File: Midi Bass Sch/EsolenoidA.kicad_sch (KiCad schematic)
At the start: 105 parts, among them Q10 BDW93C, Q11 BDW93C, Q12 BDW93C, Q13 BDW93C, Q14 BDW93C, Q15 BDW93C, Q16 BDW93C, Q17 BDW93C, Q18 BDW93C, Q19 BDW93C, Q20 BDW93C, Q21 BDW93C, Q22 BDW93C, Q23 BDW93C, Q24 BDW93C, Q25 BDW93C, Q26 BDW93C, Q27 BDW93C, Q28 BDW93C, Q9 BDW93C, U10 LTV-247, U11 LTV-247, U4 LTV-247, U8 LTV-247, U9 LTV-247

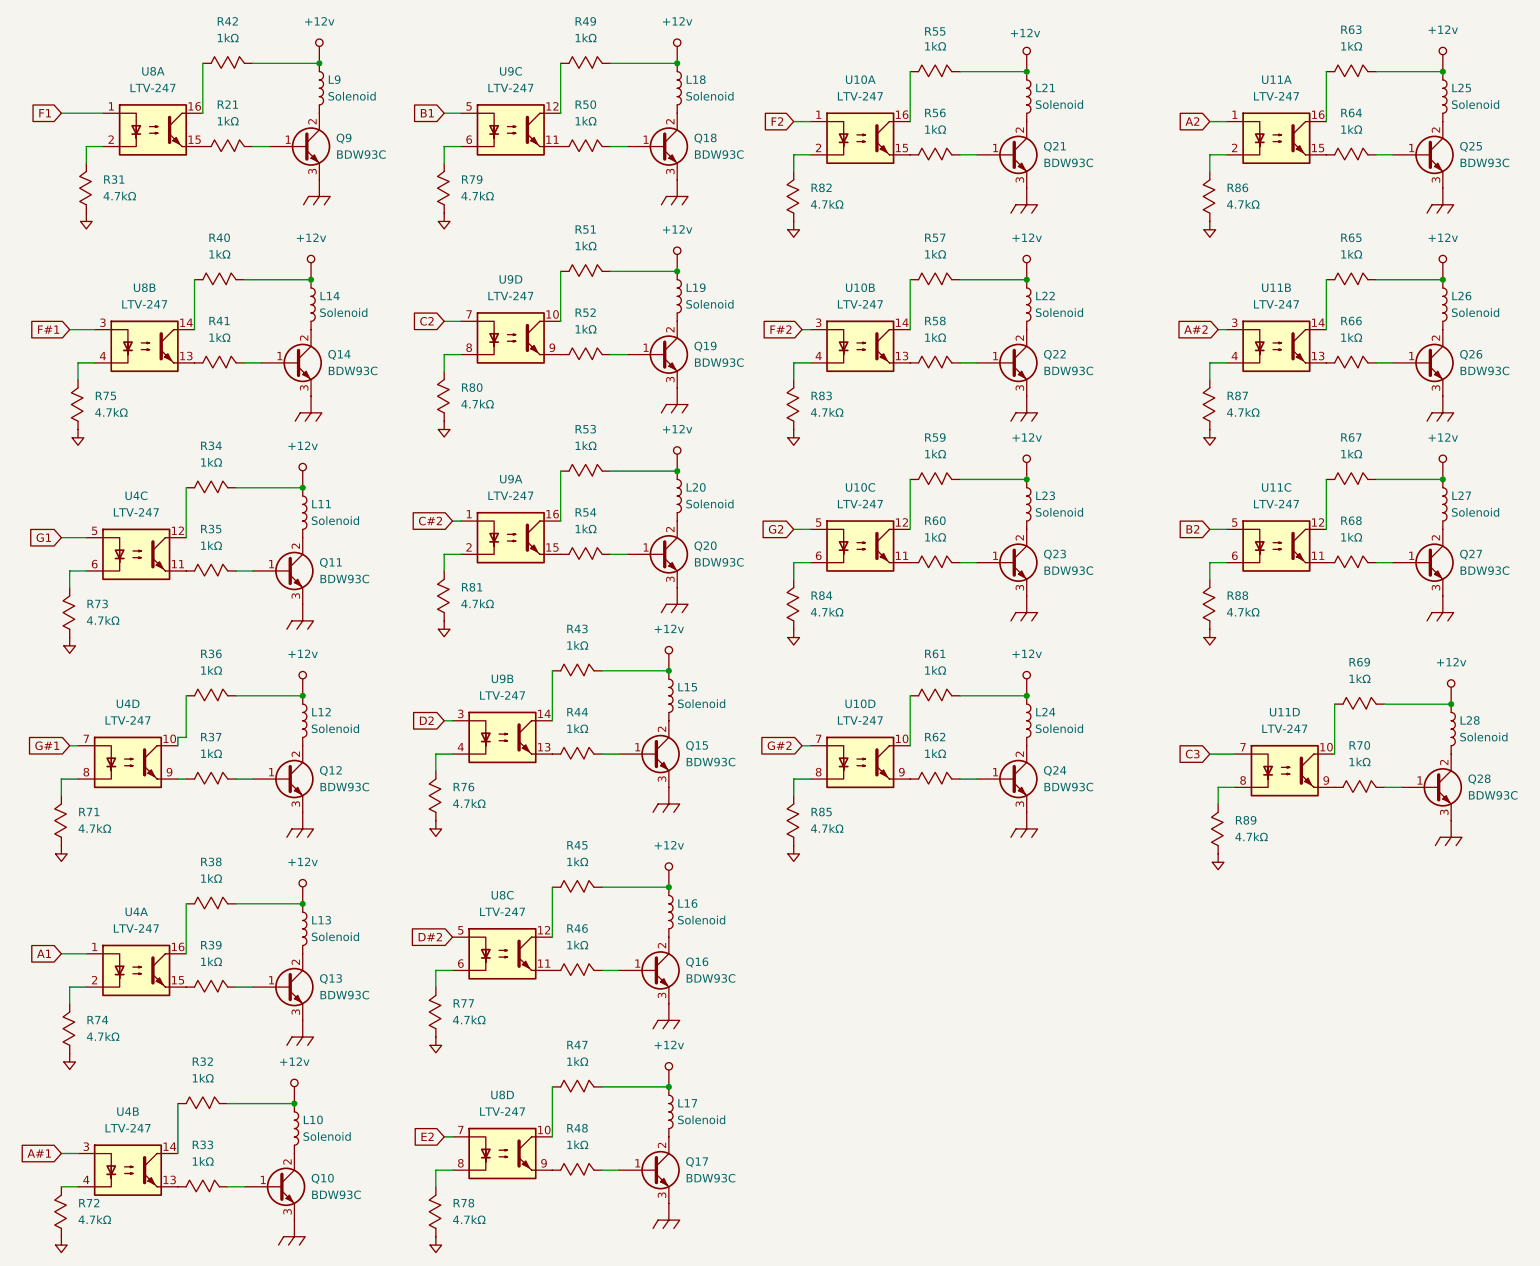
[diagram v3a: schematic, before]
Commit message: added solenoid array for the A slave
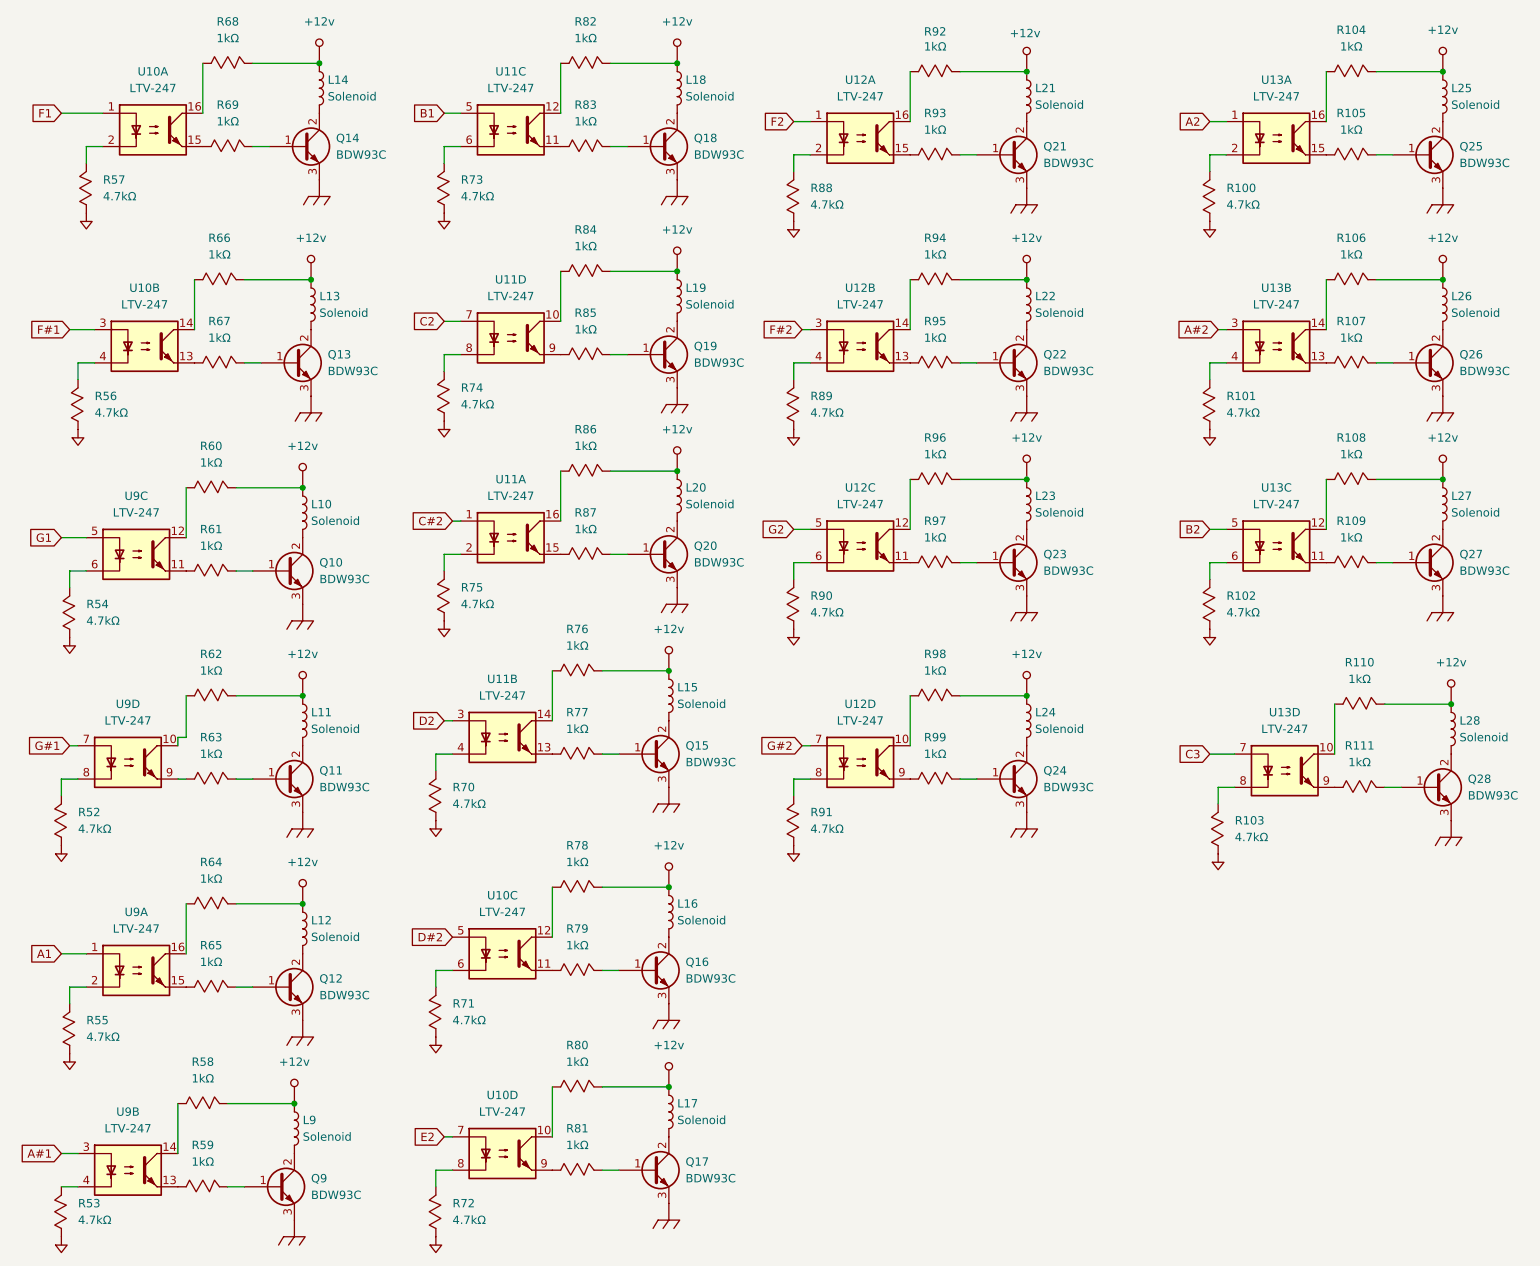
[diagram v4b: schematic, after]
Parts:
- renumbered L11 to L10, L12 to L11, L13 to L12, L14 to L13, L9 to L14, L10 to L9, Q11 to Q10, Q12 to Q11, Q13 to Q12, Q14 to Q13, Q9 to Q14, Q10 to Q9, R86 to R100, R87 to R101, R88 to R102, R89 to R103, R63 to R104, R64 to R105, R65 to R106, R66 to R107, R67 to R108, R68 to R109, R69 to R110, R70 to R111, R71 to R52, R72 to R53, R73 to R54, R74 to R55, R75 to R56, R31 to R57, R32 to R58, R33 to R59, R34 to R60, R35 to R61, R36 to R62, R37 to R63, R38 to R64, R39 to R65, R40 to R66, R41 to R67, R42 to R68, R21 to R69, R76 to R70, R77 to R71, R78 to R72, R79 to R73, R80 to R74, R81 to R75, R43 to R76, R44 to R77, R45 to R78, R46 to R79, R47 to R80, R48 to R81, R49 to R82, R50 to R83, R51 to R84, R52 to R85, R53 to R86, R54 to R87, R82 to R88, R83 to R89, R84 to R90, R85 to R91, R55 to R92, R56 to R93, R57 to R94, R58 to R95, R59 to R96, R60 to R97, R61 to R98, R62 to R99, U8 to U10, U9 to U11, U10 to U12, U11 to U13, U4 to U9

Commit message: added solenoid array for the G slave
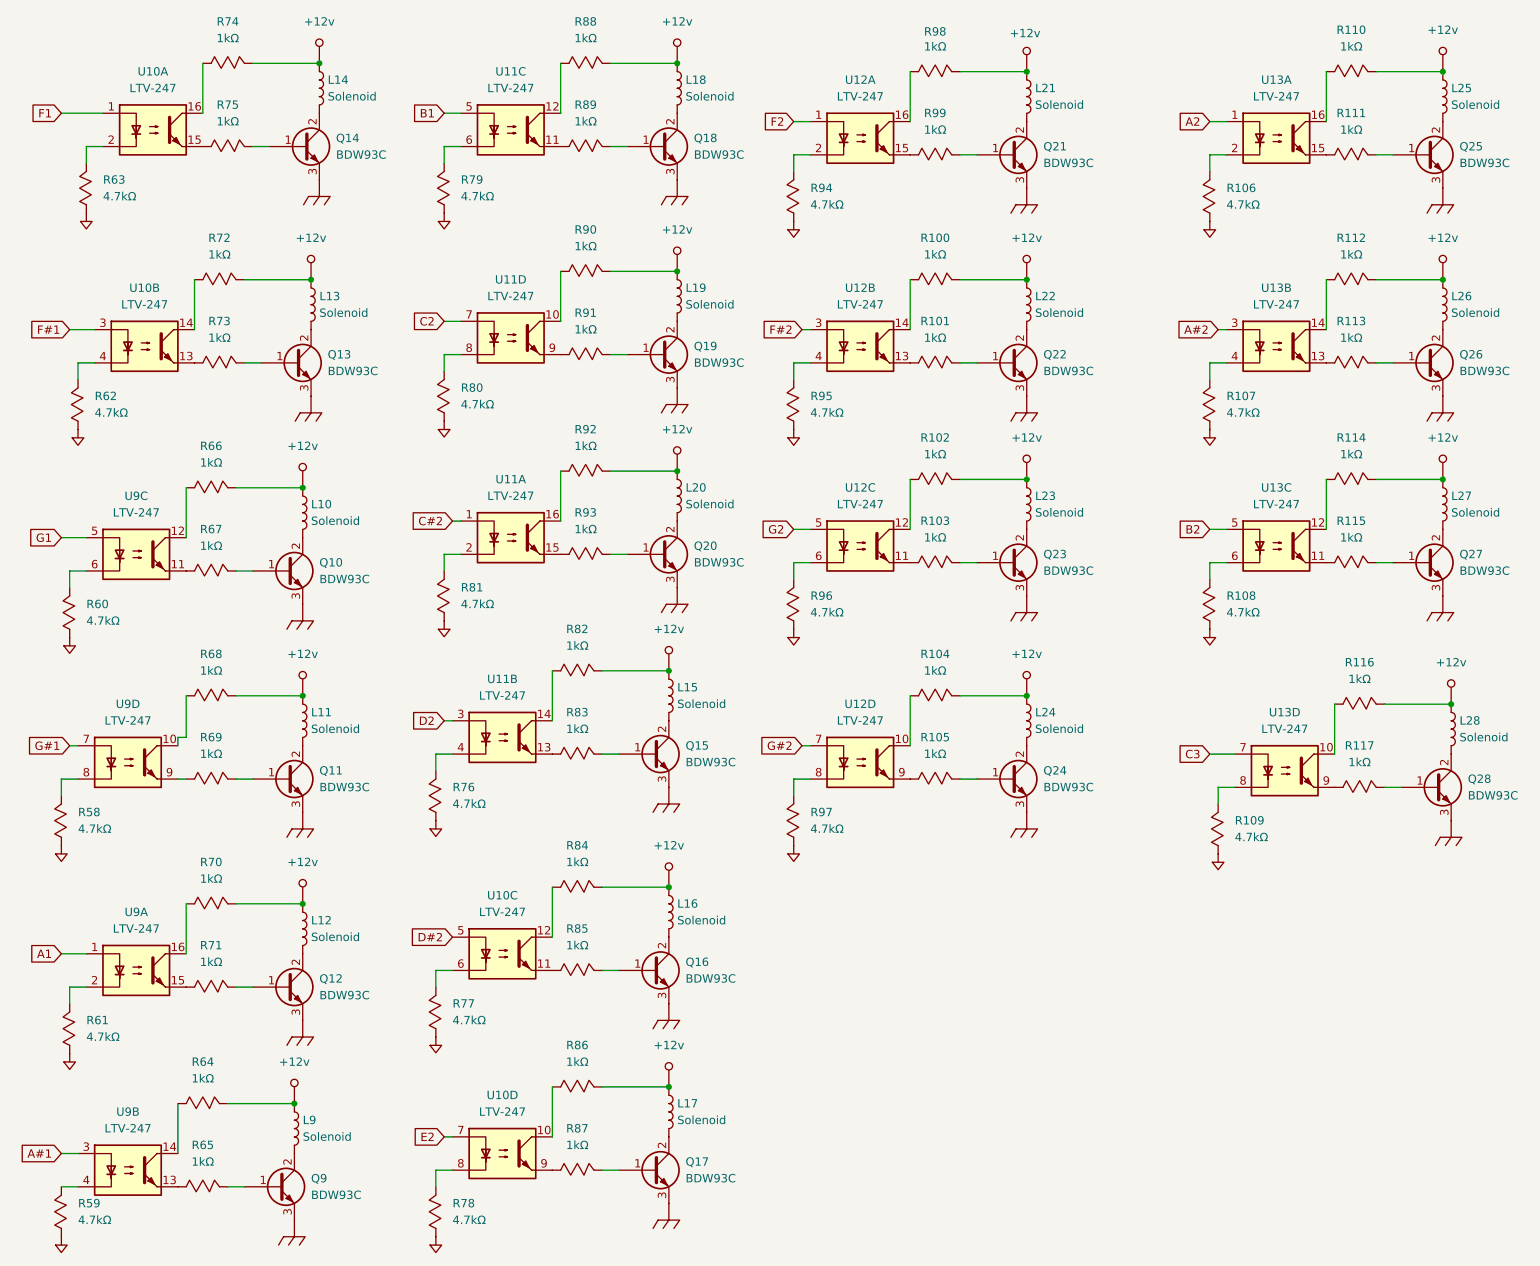
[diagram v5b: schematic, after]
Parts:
- renumbered R94 to R100, R95 to R101, R96 to R102, R97 to R103, R98 to R104, R99 to R105, R100 to R106, R101 to R107, R102 to R108, R103 to R109, R104 to R110, R105 to R111, R106 to R112, R107 to R113, R108 to R114, R109 to R115, R110 to R116, R111 to R117, R52 to R58, R53 to R59, R54 to R60, R55 to R61, R56 to R62, R57 to R63, R58 to R64, R59 to R65, R60 to R66, R61 to R67, R62 to R68, R63 to R69, R64 to R70, R65 to R71, R66 to R72, R67 to R73, R68 to R74, R69 to R75, R70 to R76, R71 to R77, R72 to R78, R73 to R79, R74 to R80, R75 to R81, R76 to R82, R77 to R83, R78 to R84, R79 to R85, R80 to R86, R81 to R87, R82 to R88, R83 to R89, R84 to R90, R85 to R91, R86 to R92, R87 to R93, R88 to R94, R89 to R95, R90 to R96, R91 to R97, R92 to R98, R93 to R99

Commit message: added footprints to kicad schematic still need footprint for din connector
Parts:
- Q10, Q11, Q12, Q13, Q14, Q15, Q16, Q17, Q18, Q19, Q20, Q21, Q22, Q23, Q24, Q25, Q26, Q27, Q28, Q9: footprint (none) -> Package_TO_SOT_THT:TO-220-3_Vertical
- R100, R101, R102, R103, R104, R105, R106, R107, R108, R109, R110, R111, R112, R113, R114, R115, R116, R117, R58, R59, R60, R61, R62, R63, R64, R65, R66, R67, R68, R69, R70, R71, R72, R73, R74, R75, R76, R77, R78, R79, R80, R81, R82, R83, R84, R85, R86, R87, R88, R89, R90, R91, R92, R93, R94, R95, R96, R97, R98, R99: footprint (none) -> Resistor_SMD:R_0805_2012Metric_Pad1.20x1.40mm_HandSolder
